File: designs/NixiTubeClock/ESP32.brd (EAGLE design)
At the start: 43 x 54 mm, 19 parts, among them IC6 ESP32-WROVER-B

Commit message: pushed to fusion
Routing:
- added copper zone on layer 1, net GND
- added copper zone on layer 16, net GND
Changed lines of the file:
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@@
 <?xml version="1.0" encoding="utf-8"?>
 <!DOCTYPE eagle SYSTEM "eagle.dtd">
-<eagle version="9.4.2">
+<eagle version="9.5.1">
 <drawing>
 <settings>
@@
 </layers>
 <board>
+<fusionsync huburn="a.cGVyc29uYWw6dWUyYTNmMDU1" projecturn="a.cGVyc29uYWw6dWUyYTNmMDU1IzIwMTgxMjEwMTY0OTQ5MjI2" f3durn="urn:adsk.wipprod:dm.lineage:m4VszXO8RDeAbnUYYUwrcQ" pcbguid="13ce3a2b-8468-4712-b890-285fbb146dd9" lastpulledtime="" lastsyncedchangeguid="e74c5fc7-7a09-ba2e-6caf-915c2b94b0bf"/>
 <plain>
 <text x="26.046" y="20.702" size="0.889" layer="25" rot="R180">GND</text>
@@
 <wire x1="12.092" y1="33.887" x2="12.142" y2="33.837" width="0.508" layer="16"/>
 <wire x1="12.142" y1="33.837" x2="12.142" y2="31.547" width="0.508" layer="16"/>
-<wire x1="16.15" y1="38" x2="16.15" y2="39.172" width="0" layer="19" extent="1-1"/>
-<wire x1="16.15" y1="41.35" x2="16.15" y2="39.172" width="0" layer="19" extent="1-1"/>
+<polygon width="0.1524" layer="1">
+<vertex x="-5" y="51"/>
+<vertex x="38" y="51"/>
+<vertex x="38" y="-3"/>
+<vertex x="-5" y="-3"/>
+</polygon>
+<polygon width="0.1524" layer="16">
+<vertex x="-5" y="51"/>
+<vertex x="38" y="51"/>
+<vertex x="38" y="-3"/>
+<vertex x="-5" y="-3"/>
+</polygon>
 </signal>
 <signal name="3.3V">
@@
 </note>
 <note version="8.3" severity="warning">
+Since Version 8.3, EAGLE supports Fusion synchronisation.
+This feature will not be available in this version and saving
+the document will break the link to the Fusion PCB feature.
+</note>
+<note version="8.3" severity="warning">

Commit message: added parts for nixi clock final check during the week
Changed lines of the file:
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@@
 <setting verticaltext="up"/>
 </settings>
-<grid distance="1" unitdist="mm" unit="mm" style="lines" multiple="1" display="yes" altdistance="5" altunitdist="mil" altunit="mil"/>
+<grid distance="0.1" unitdist="mm" unit="mm" style="lines" multiple="1" display="yes" altdistance="5" altunitdist="mil" altunit="mil"/>
 <layers>
 <layer number="1" name="Top" color="4" fill="1" visible="yes" active="yes"/>
@@
 </layers>
 <board>
-<fusionsync huburn="a.cGVyc29uYWw6dWUyYTNmMDU1" projecturn="a.cGVyc29uYWw6dWUyYTNmMDU1IzIwMTgxMjEwMTY0OTQ5MjI2" f3durn="urn:adsk.wipprod:dm.lineage:m4VszXO8RDeAbnUYYUwrcQ" pcbguid="13ce3a2b-8468-4712-b890-285fbb146dd9" lastpulledtime="" lastsyncedchangeguid="e74c5fc7-7a09-ba2e-6caf-915c2b94b0bf"/>
+<fusionsync huburn="a.cGVyc29uYWw6dWUyYTNmMDU1" projecturn="a.cGVyc29uYWw6dWUyYTNmMDU1IzIwMTgxMjEwMTY0OTQ5MjI2" f3durn="urn:adsk.wipprod:dm.lineage:m4VszXO8RDeAbnUYYUwrcQ" pcbguid="13ce3a2b-8468-4712-b890-285fbb146dd9" lastpulledtime="" lastsyncedchangeguid="0621ef2d-4e75-c352-c05d-c6989f4fbca6"/>
 <plain>
 <text x="26.046" y="20.702" size="0.889" layer="25" rot="R180">GND</text>
@@
 <text x="10.75" y="16" size="0.4064" layer="26" rot="MR270">GPIO12</text>
 <text x="8.25" y="16" size="0.4064" layer="26" rot="MR270">GPIO14</text>
+<text x="-2" y="44.8" size="1.016" layer="25">GND</text>
+<text x="-2" y="42.2" size="1.016" layer="25">3.3V</text>
 </plain>
 <attributes>

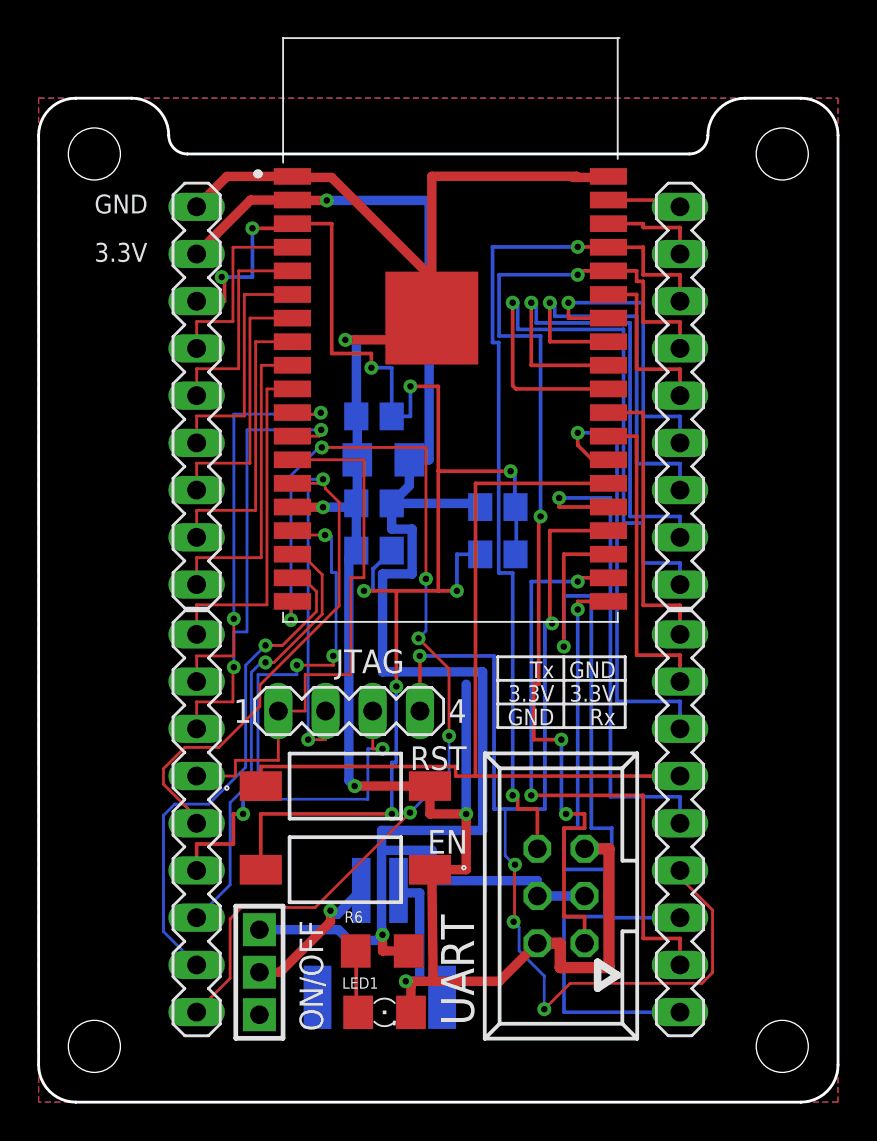
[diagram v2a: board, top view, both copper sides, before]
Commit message: changed ESP32 on/off switch distance to pins
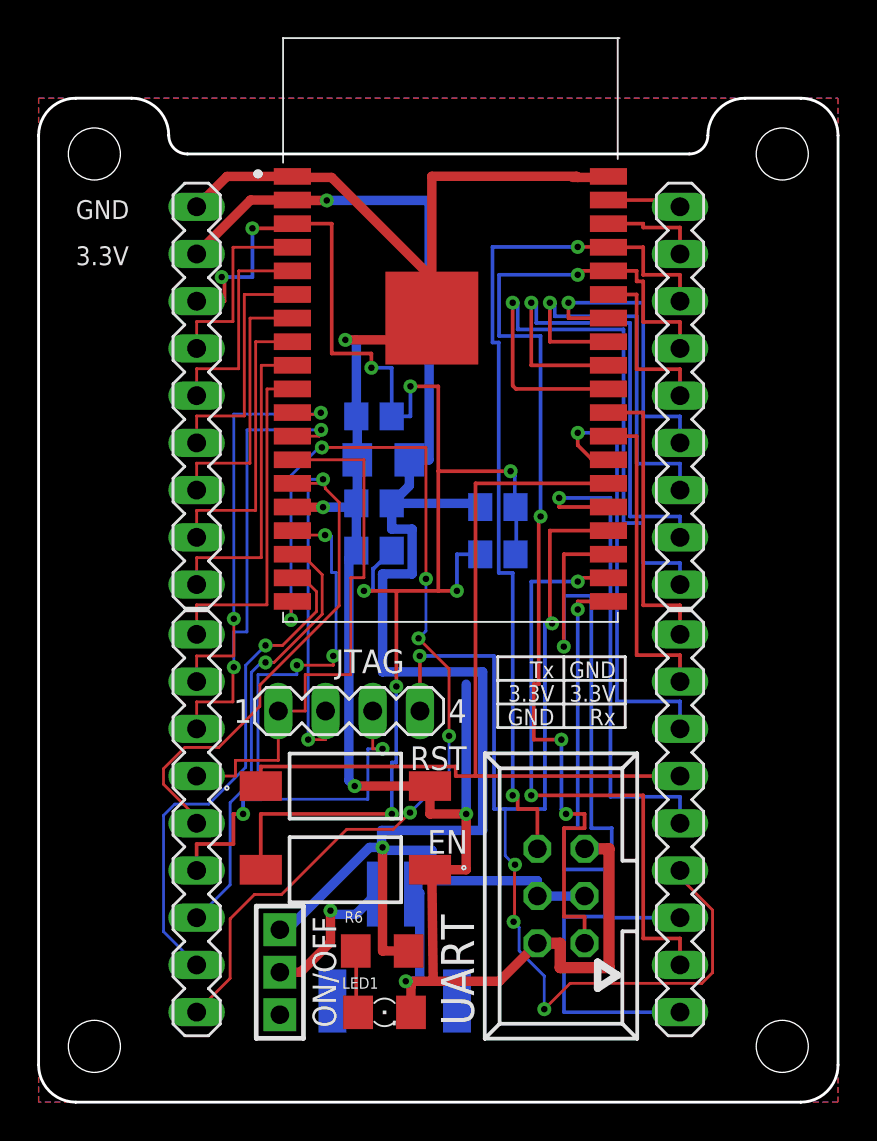
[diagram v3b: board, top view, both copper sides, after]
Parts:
- moved ON/OFF 1.10 mm to (7.72, 3.48)
- moved POWER 0.82 mm to (14.2, 8.19)
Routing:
- net GND: track 121.3 -> 120.5 mm
- net 3.3V: track 95.7 -> 96.3 mm

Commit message: started work on mainboard
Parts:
- moved C1 0.50 mm to (12.5, 33.9)
- moved C2 0.50 mm to (13.0, 31.5)
- moved C3 0.50 mm to (12.5, 29.2)
- moved C4 0.50 mm to (12.5, 26.7)
- moved EN 0.50 mm to (11.0, 9.50)
- moved IC6 0.50 mm to (16.0, 38.5)
- moved JTAG 0.50 mm to (11.2, 18.0)
- moved LED1 0.50 mm to (13.1, 1.83)
- moved ON/OFF 0.50 mm to (7.22, 3.48)
- moved POWER 0.50 mm to (13.7, 8.19)
- moved R1 0.50 mm to (19.2, 29.0)
- moved R2 0.50 mm to (19.2, 26.5)
- moved R6 0.50 mm to (13.0, 5.13)
- moved RST 0.50 mm to (11.0, 14.0)
- moved SV1 0.50 mm to (29.0, 12.0)
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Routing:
- net EN: track 83.3 -> 87.7 mm
- net GND: track 120.5 -> 122.8 mm
- net 3.3V: track 96.3 -> 98.1 mm
- net GPIO15: track 64.4 -> 66.0 mm
- net RXD0: track 57.5 -> 56.2 mm
- net SD2: track 23.7 -> 24.8 mm
- net IO27: track 24.8 -> 25.9 mm
- net TXD0: track 47.8 -> 46.8 mm
- net GPIO14: track 29.9 -> 30.9 mm
- net CLK: track 35.2 -> 34.2 mm
- net CMD: track 56.1 -> 55.5 mm
- net IO26: track 22.9 -> 22.4 mm
- net IO0: track 47.0 -> 46.5 mm
- net GPIO13: track 40.3 -> 40.8 mm
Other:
- board size 43 x 54 mm -> 32 x 47.5 mm

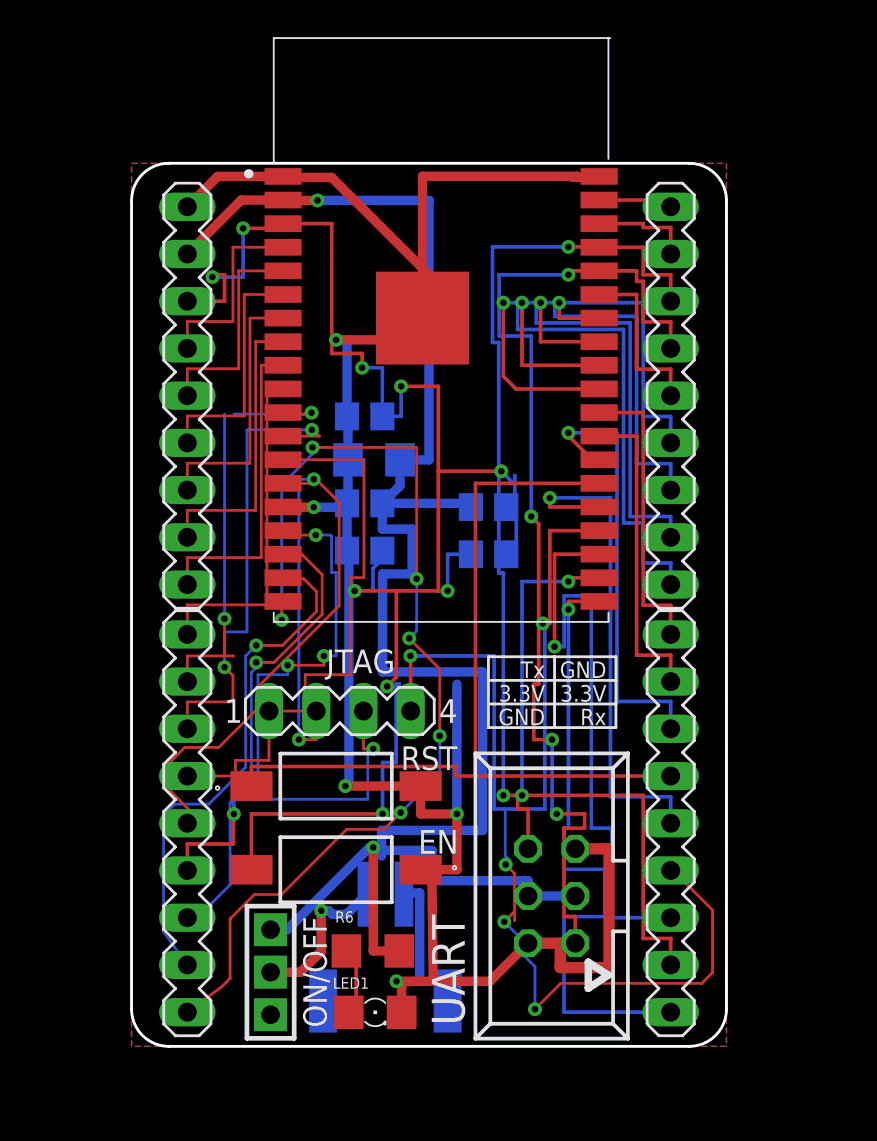
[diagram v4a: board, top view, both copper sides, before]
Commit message: added work to mainboard LEDs N-Channel Mosfet and names tNames
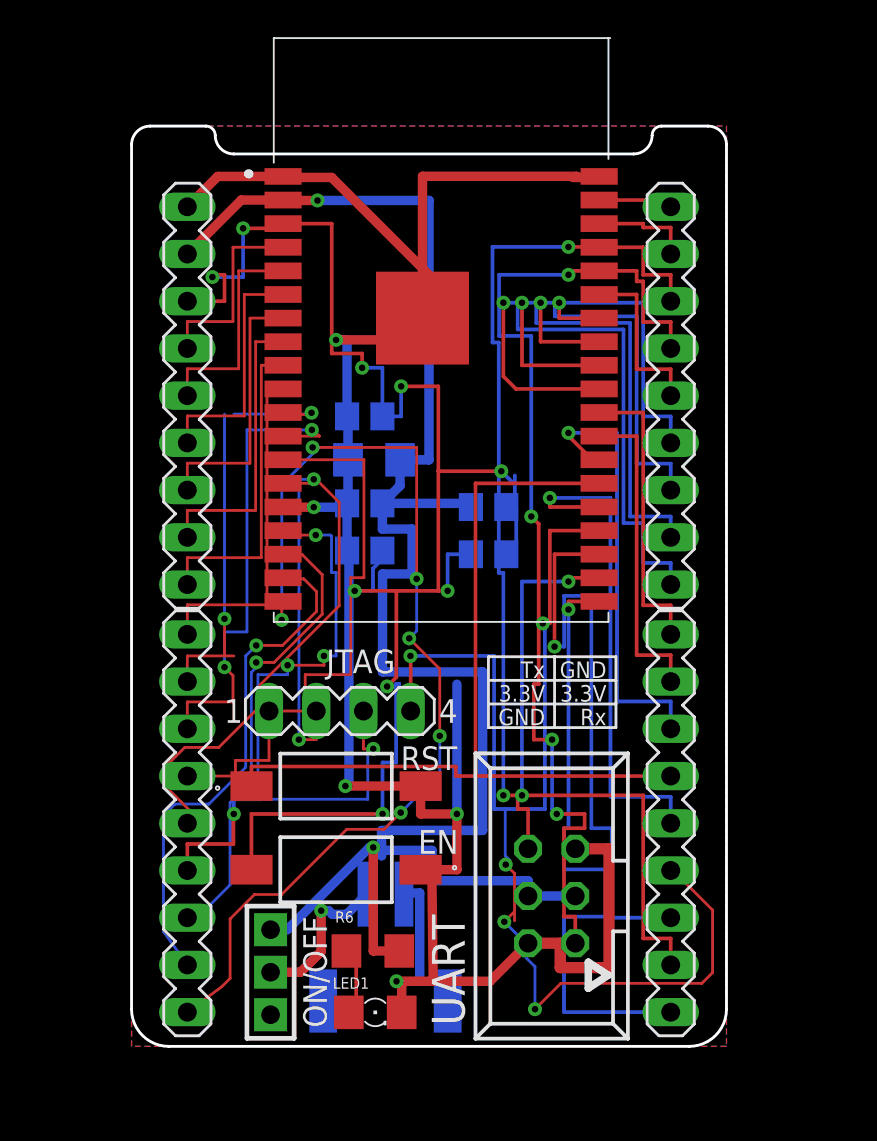
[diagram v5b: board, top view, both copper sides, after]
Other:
- board size 32 x 47.5 mm -> 32 x 49.5 mm
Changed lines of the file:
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@@
 <drawing>
 <settings>
-<setting alwaysvectorfont="yes"/>
+<setting alwaysvectorfont="no"/>
 <setting verticaltext="up"/>
 </settings>
@@
 </layers>
 <board>
-<fusionsync huburn="a.cGVyc29uYWw6dWUyYTNmMDU1" projecturn="a.cGVyc29uYWw6dWUyYTNmMDU1IzIwMTgxMjEwMTY0OTQ5MjI2" f3durn="urn:adsk.wipprod:dm.lineage:m4VszXO8RDeAbnUYYUwrcQ" pcbguid="13ce3a2b-8468-4712-b890-285fbb146dd9" lastpulledtime="" lastsyncedchangeguid="01f02148-267c-ac4a-df02-37f874a70fa3"/>
+<fusionsync huburn="a.cGVyc29uYWw6dWUyYTNmMDU1" projecturn="a.cGVyc29uYWw6dWUyYTNmMDU1IzIwMTgxMjEwMTY0OTQ5MjI2" f3durn="urn:adsk.wipprod:dm.lineage:m4VszXO8RDeAbnUYYUwrcQ" pcbguid="13ce3a2b-8468-4712-b890-285fbb146dd9" lastpulledtime="" lastsyncedchangeguid="05052b95-acb4-8089-79fe-d2d8dda834dc"/>
 <plain>
 <text x="25.546" y="20.702" size="0.889" layer="25" rot="R180">GND</text>
@@
 <text x="5" y="45" size="1.016" layer="26">GND</text>
 <text x="5" y="42.5171" size="1.016" layer="26">3.3V</text>
-<wire x1="0" y1="45.5" x2="0" y2="2" width="0.1524" layer="20"/>
+<wire x1="28.5" y1="49.5" x2="31" y2="49.5" width="0.1524" layer="20"/>
+<wire x1="31" y1="49.5" x2="32" y2="48.5" width="0.1524" layer="20" curve="-90"/>
+<wire x1="32" y1="48.5" x2="32" y2="2" width="0.1524" layer="20"/>
+<wire x1="0" y1="2" x2="0" y2="48.5" width="0.1524" layer="20"/>
+<wire x1="0" y1="48.5" x2="1" y2="49.5" width="0.1524" layer="20" curve="-90"/>
+<wire x1="1" y1="49.5" x2="4" y2="49.5" width="0.1524" layer="20"/>
+<wire x1="4" y1="49.5" x2="4.5" y2="49" width="0.1524" layer="20" curve="-90"/>
 <wire x1="0" y1="2" x2="2" y2="0" width="0.1524" layer="20" curve="90"/>
 <wire x1="2" y1="0" x2="30" y2="0" width="0.1524" layer="20"/>
 <wire x1="30" y1="0" x2="32" y2="2" width="0.1524" layer="20" curve="90"/>
-<wire x1="32" y1="2" x2="32" y2="45.5" width="0.1524" layer="20"/>
-<wire x1="32" y1="45.5" x2="30" y2="47.5" width="0.1524" layer="20" curve="90"/>
-<wire x1="30" y1="47.5" x2="2" y2="47.5" width="0.1524" layer="20"/>
-<wire x1="2" y1="47.5" x2="0" y2="45.5" width="0.1524" layer="20" curve="90"/>
+<wire x1="4.5" y1="49" x2="5.5" y2="48" width="0.1524" layer="20" curve="90"/>
+<wire x1="5.5" y1="48" x2="27" y2="48" width="0.1524" layer="20"/>
+<wire x1="27" y1="48" x2="28" y2="49" width="0.1524" layer="20" curve="90"/>
+<wire x1="28" y1="49" x2="28.5" y2="49.5" width="0.1524" layer="20" curve="-90"/>
 </plain>
 <attributes>
@@
 <wire x1="11.642" y1="33.837" x2="11.642" y2="31.547" width="0.508" layer="16"/>
 <polygon width="0.1524" layer="1">
-<vertex x="0" y="47.5"/>
-<vertex x="32" y="47.5"/>
-<vertex x="32" y="0"/>
 <vertex x="0" y="0"/>
+<vertex x="0" y="48.5" curve="-90"/>
+<vertex x="1" y="49.5"/>
+<vertex x="32" y="49.5"/>
+<vertex x="32" y="0"/>
 </polygon>
 <polygon width="0.1524" layer="16">
-<vertex x="0" y="47.5"/>
-<vertex x="32" y="47.5"/>
-<vertex x="32" y="0"/>
 <vertex x="0" y="0"/>
+<vertex x="0" y="48.5" curve="-90"/>
+<vertex x="1" y="49.5"/>
+<vertex x="32" y="49.5"/>
+<vertex x="32" y="0"/>
 </polygon>
 <wire x1="25.15" y1="46.792" x2="25.646" y2="46.738" width="0" layer="19" extent="1-1"/>

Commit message: integrated T/H sensor
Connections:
- net N$1: now also ON/OFF.P$3; no longer ON/OFF.P$2
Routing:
- net N$1: track 8.37 -> 10.8 mm
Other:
- board text added: "IO23"
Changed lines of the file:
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@@
 </layers>
 <board>
-<fusionsync huburn="a.cGVyc29uYWw6dWUyYTNmMDU1" projecturn="a.cGVyc29uYWw6dWUyYTNmMDU1IzIwMTgxMjEwMTY0OTQ5MjI2" f3durn="urn:adsk.wipprod:dm.lineage:m4VszXO8RDeAbnUYYUwrcQ" pcbguid="13ce3a2b-8468-4712-b890-285fbb146dd9" lastpulledtime="" lastsyncedchangeguid="05052b95-acb4-8089-79fe-d2d8dda834dc"/>
+<fusionsync huburn="a.cGVyc29uYWw6dWUyYTNmMDU1" projecturn="a.cGVyc29uYWw6dWUyYTNmMDU1IzIwMTgxMjEwMTY0OTQ5MjI2" f3durn="urn:adsk.wipprod:dm.lineage:m4VszXO8RDeAbnUYYUwrcQ" pcbguid="13ce3a2b-8468-4712-b890-285fbb146dd9" lastpulledtime="" lastsyncedchangeguid="94207021-e932-fb7c-ae7e-b07de7dc214e"/>
 <plain>
 <text x="25.546" y="20.702" size="0.889" layer="25" rot="R180">GND</text>
@@
 <wire x1="27" y1="48" x2="28" y2="49" width="0.1524" layer="20" curve="90"/>
 <wire x1="28" y1="49" x2="28.5" y2="49.5" width="0.1524" layer="20" curve="-90"/>
+<text x="0.5" y="47" size="1.016" layer="25">GND</text>
+<text x="28.5" y="47" size="1.016" layer="25">IO23</text>
 </plain>
 <attributes>
@@
 <vertex x="32" y="0"/>
 </polygon>
-<wire x1="25.15" y1="46.792" x2="25.646" y2="46.738" width="0" layer="19" extent="1-1"/>
-<wire x1="15.65" y1="38" x2="15.65" y2="39.172" width="0" layer="19" extent="1-1"/>
-<wire x1="11.692" y1="26.267" x2="11.692" y2="26.567" width="0" layer="19" extent="16-16"/>
-<wire x1="16.15" y1="41.35" x2="15.65" y2="39.172" width="0" layer="19" extent="1-1"/>
 </signal>
 <signal name="3.3V">
@@
 <signal name="N$1">
 <contactref element="POWER" pad="2"/>
-<contactref element="ON/OFF" pad="P$2"/>
-<wire x1="12.654" y1="8.187" x2="11.567" y2="7.1" width="0.508" layer="16"/>
-<wire x1="11.567" y1="7.1" x2="10.8" y2="7.1" width="0.508" layer="16"/>
-<wire x1="10.8" y1="7.1" x2="10.6" y2="7.3" width="0.508" layer="16"/>
-<wire x1="10.6" y1="7.3" x2="10.2" y2="7.3" width="0.508" layer="16"/>
-<via x="10.2" y="7.3" extent="1-16" drill="0.35"/>
-<wire x1="10.2" y1="7.3" x2="10.2" y2="5.1" width="0.508" layer="1"/>
-<wire x1="9.088" y1="3.988" x2="7.477" y2="3.988" width="0.508" layer="1"/>
-<wire x1="10.2" y1="5.1" x2="9.088" y2="3.988" width="0.508" layer="1"/>
+<contactref element="ON/OFF" pad="P$3"/>
+<wire x1="7.477" y1="1.702" x2="7.775" y2="2" width="0.4064" layer="1"/>
+<wire x1="7.775" y1="2" x2="10" y2="2" width="0.4064" layer="1"/>
+<wire x1="10" y1="2" x2="10" y2="6.5" width="0.4064" layer="1"/>
+<wire x1="10" y1="6.5" x2="11" y2="7.5" width="0.4064" layer="1"/>
+<wire x1="11" y1="7.5" x2="12.2154" y2="7.5" width="0.4064" layer="1"/>
+<wire x1="12.2154" y1="7.5" x2="12.3904" y2="7.5" width="0.4064" layer="1"/>
+<via x="12.2154" y="7.5" extent="1-16" drill="0.35"/>
+<wire x1="12.2154" y1="7.5" x2="12.654" y2="7.9386" width="0.4064" layer="16"/>
+<wire x1="12.654" y1="7.9386" x2="12.654" y2="8.187" width="0.4064" layer="16"/>
 </signal>
 </signals>
